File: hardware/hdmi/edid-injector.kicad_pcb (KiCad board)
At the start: 2 copper layers, 42 parts, among them SW1 SW_PUSH, U1 C8051F381/3/5/7/C-GQ

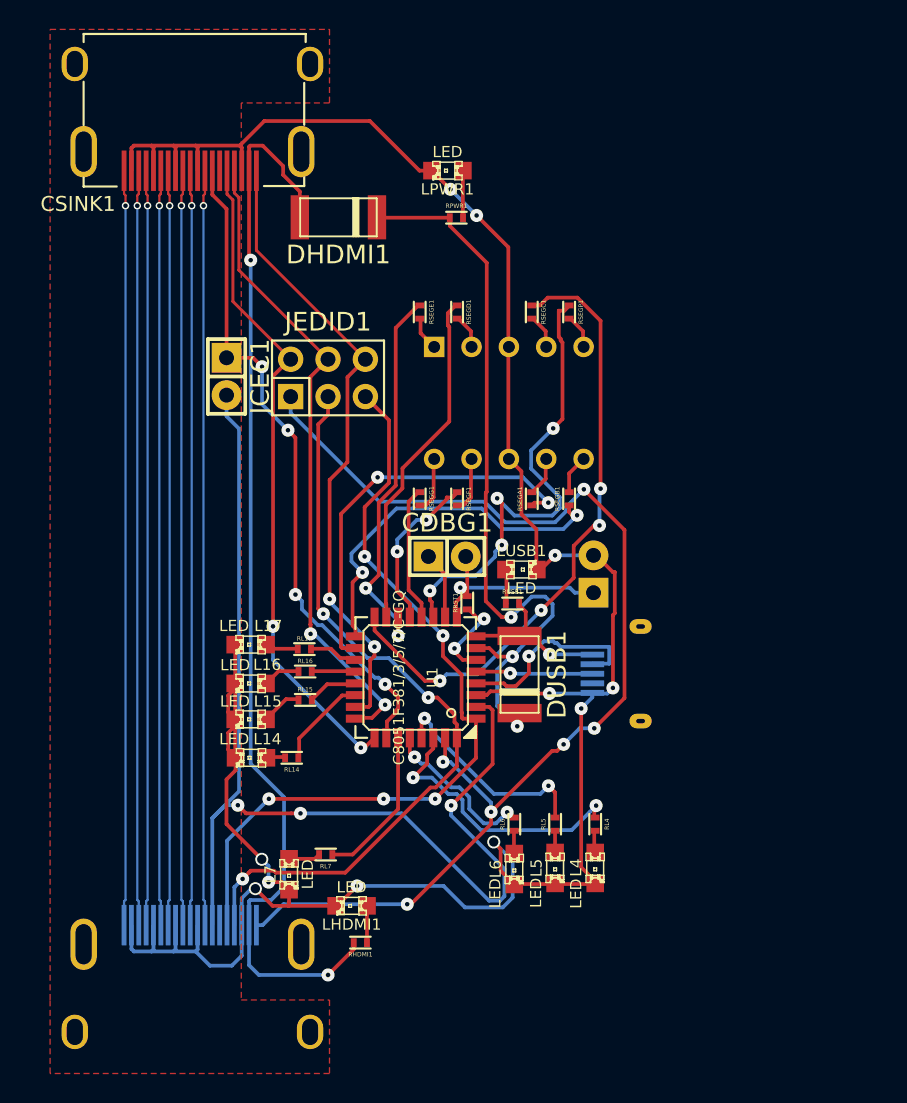
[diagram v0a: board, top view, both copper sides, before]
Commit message: Fixing component assignments.
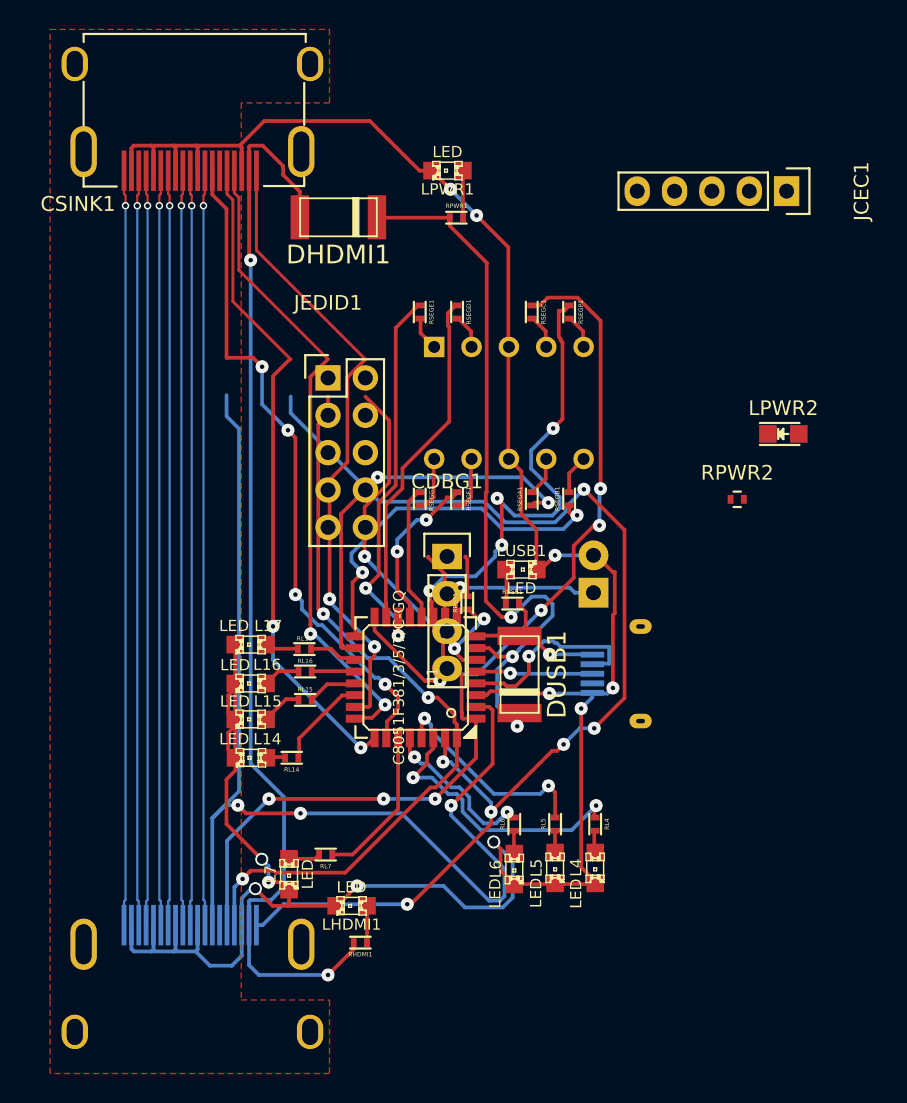
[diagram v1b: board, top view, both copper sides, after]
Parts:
- added LPWR2: LED, LEDs:LED_0805, F.Cu at (144.1, 83.1)
- added RPWR2: R, Resistors_SMD:R_0402, F.Cu at (140.9, 87.5)
- CDBG1: value CONN_01X02 -> CONN_01X04; footprint Pin_Headers:Pin_Header_Straight_1x02 -> Pin_Headers:Pin_Header_Straight_1x04
- JCEC1: value CONN_01X02 -> CONN_01X05; footprint Pin_Headers:Pin_Header_Straight_1x02 -> Pin_Headers:Pin_Header_Straight_1x05
- JEDID1: value CONN_02X03 -> CONN_02X05; footprint Pin_Headers:Pin_Header_Straight_2x03 -> Pin_Headers:Pin_Header_Straight_2x05
- moved JCEC1 40.1 mm to (144.3, 66.5)
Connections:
- CDBG1 pad 1: Net-(CDBG1-Pad1) -> GND
- CSINK1 pad 14: Net-(CSINK1-Pad14) -> /RES
- CSRC1 pad 14: Net-(CSRC1-Pad14) -> /RES
- JCEC1 pad 1: /SINK_CEC -> Net-(JCEC1-Pad1)
- U1 pad 10: Net-(CDBG1-Pad1) -> Net-(CDBG1-Pad3)
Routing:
- net /VCC3V3: track 6.17 -> 46.5 mm, vias 2 -> 6
- net Net-(RSEGC1-Pad1): track 42.8 -> 4.23 mm, vias 4 -> 0
- net /SINK_HPD: track 42.9 -> 6.32 mm, vias 2 -> 0
- net GND: track 178.7 -> 215.3 mm, vias 11 -> 13
- net Net-(CDBG1-Pad3): track 0.00 -> 25.8 mm, vias 0 -> 2
- net /SRC_SCL: track 54.6 -> 31.6 mm, vias 5 -> 3
- net Net-(CDBG1-Pad1): track 4.62 -> 0.00 mm

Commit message: First PCB design from Phyllis.
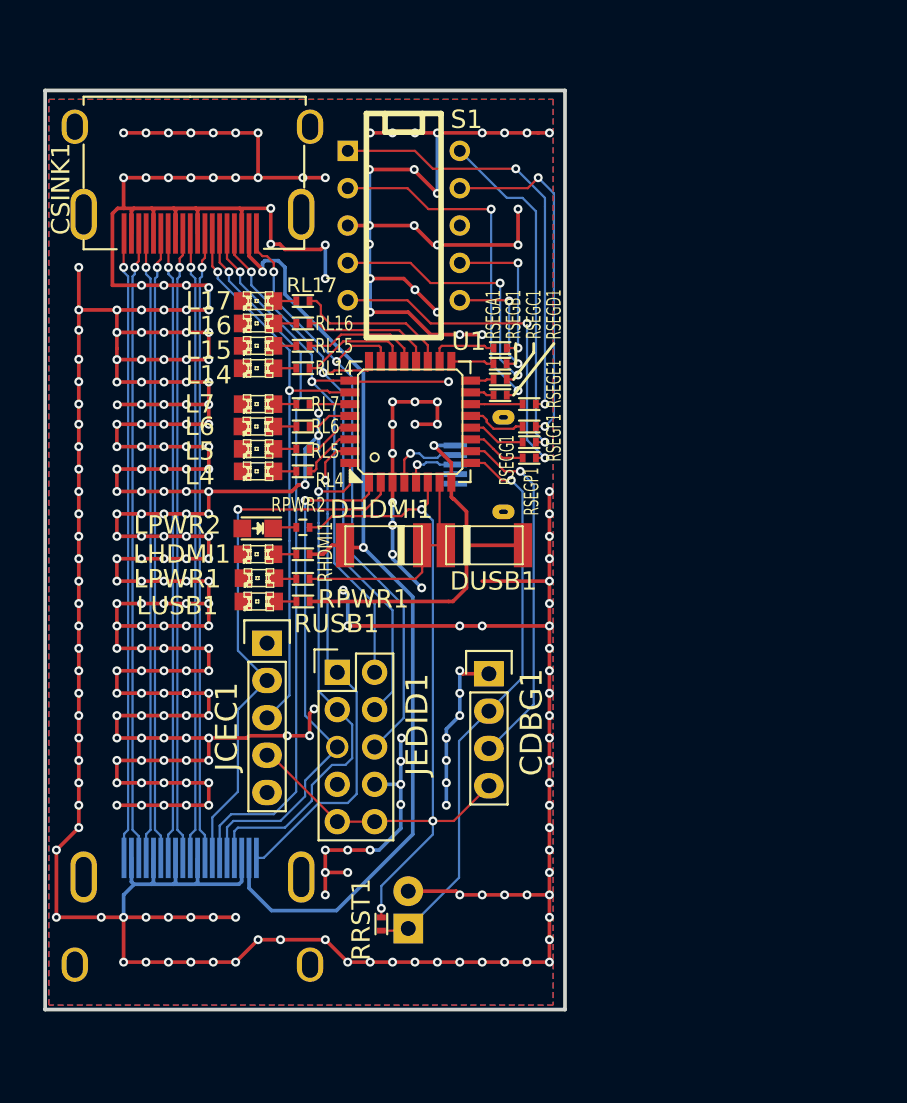
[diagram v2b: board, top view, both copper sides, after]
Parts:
- S1: moved to F.Cu
- moved JCEC1 46.8 mm to (108.9, 97.3), turned to 0 degrees
- moved LPWR2 36.3 mm to (108.3, 89.5), turned to 180 degrees
- moved L4 35.4 mm to (108.3, 85.6), turned to 180 degrees
- moved L5 34.9 mm to (108.3, 84.1), turned to 180 degrees
- moved L6 34.8 mm to (108.3, 82.5), turned to 180 degrees
- moved L7 32.0 mm to (108.3, 81.0), turned to 180 degrees
- moved RL4 31.2 mm to (111.4, 85.6), turned to 180 degrees
- moved RL5 30.7 mm to (111.4, 84.1), turned to 180 degrees
- moved RL7 30.7 mm to (111.4, 81.0)
- moved RL6 30.6 mm to (111.4, 82.5), turned to 180 degrees
- moved LPWR1 30.5 mm to (108.4, 92.9)
- moved RPWR2 29.6 mm to (111.4, 89.4)
- moved RHDMI1 26.7 mm to (111.4, 91.2), turned to 0 degrees
- moved RPWR1 26.7 mm to (111.4, 92.9), turned to 180 degrees
- moved RL14 26.5 mm to (111.4, 78.6)
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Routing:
- net GND: track 215.3 -> 555.9 mm, vias 13 -> 279
- net /RES: track 0.00 -> 48.7 mm, vias 0 -> 1
- net /SRC_HPD: track 79.2 -> 34.0 mm, vias 6 -> 1
- net /SRC_CEC: track 76.7 -> 37.1 mm, vias 3 -> 1
- net /SINK_HPD: track 6.32 -> 44.5 mm, vias 0 -> 2
- net /VCC5V0: track 52.2 -> 15.8 mm, vias 3 -> 0
- net Net-(RSEGP1-Pad1): track 32.7 -> 4.12 mm, vias 4 -> 0
- net Net-(RSEGE1-Pad2): track 2.40 -> 29.4 mm, vias 0 -> 2
- net Net-(CDBG1-Pad2): track 14.8 -> 39.2 mm
- net Net-(RSEGE1-Pad1): track 26.2 -> 3.56 mm, vias 2 -> 0
- net Net-(RSEGA1-Pad1): track 27.1 -> 4.71 mm, vias 2 -> 0
- net Net-(RSEGB1-Pad1): track 25.0 -> 2.92 mm, vias 2 -> 0
- net Net-(RSEGD1-Pad2): track 2.40 -> 24.3 mm, vias 0 -> 2
- net Net-(RSEGD1-Pad1): track 23.4 -> 1.64 mm
- net Net-(RSEGP1-Pad2): track 2.40 -> 23.1 mm, vias 0 -> 2
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- added copper zone on B.Cu, net GND
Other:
- board outline added: 35.3 x 62.5 mm
- net class Default: clearance 0.2032 -> 0.1524; trace_width 0.2032 -> 0.1524; via_dia 0.508 -> 0.6096
- net class HighSpeed: via_dia 0.508 -> 0.6096
- net class PWR: trace_width 0.6095 -> 0.25; via_dia 1 -> 0.6096; via_drill 0.635 -> 0.3048
- rule trace_clearance: 0.2032 -> 0.1524
- rule via_min_size: 0.508 -> 0.6096
- board text added: "35.35 mm"
- board text added: "62.50 mm"

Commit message: Trying to make things a little more uniform.
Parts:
- L14, L15, L16, L17, L4, L5, L6, L7, LHDMI1, LPWR1, LUSB1: footprint LEDs:LED-0805 -> LEDs:LED_0805
- RHDMI1, RL14, RL15, RL16, RL17, RL4, RL5, RL6, RL7, RPWR1, RPWR2, RRST1, RSEGA1, RSEGB1, RSEGC1, RSEGD1, RSEGE1, RSEGF1, RSEGG1, RSEGP1, RUSB1: footprint Resistors_SMD:R_0402 -> random:R_0402
- moved LUSB1 0.24 mm to (108.4, 94.2)
- moved RUSB1 0.24 mm to (111.4, 94.2)
- moved RPWR1 0.23 mm to (111.4, 92.7)
- moved RPWR2 0.23 mm to (111.4, 89.6)
- moved LPWR1 0.17 mm to (108.4, 92.7)
- moved LPWR2 0.17 mm to (108.4, 89.6)
- moved LHDMI1 0.09 mm to (108.4, 91.2)
- moved RHDMI1 0.08 mm to (111.4, 91.2)
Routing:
- net /VHDMI: track 67.7 -> 67.0 mm
- net /VCC5V0: track 15.8 -> 15.1 mm

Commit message: Tweaking.
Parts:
- moved JEDID1 2.03 mm to (114.0, 97.3)
- moved CDBG1 0.47 mm to (124.2, 99.8)
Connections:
- JCEC1 pad 4: /VCC3V3 -> GND
- JCEC1 pad 5: GND -> /VCC3V3
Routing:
- net GND: track 555.9 -> 537.8 mm, vias 279 -> 269
- net /VCC3V3: track 58.0 -> 69.4 mm, vias 3 -> 13
- net /SINK_HPD: track 44.5 -> 42.4 mm
- net /SINK_SCL: track 43.4 -> 41.5 mm
- net /SINK_SDA: track 40.8 -> 39.1 mm
- net /SRC_HPD: track 34.0 -> 35.2 mm
